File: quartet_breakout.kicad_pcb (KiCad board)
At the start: 2 copper layers, 25.4 x 53.3 mm, 3 parts, among them J1 QUARTET_RECV, J2 QUARTET_RECV, J5 Conn_01x18

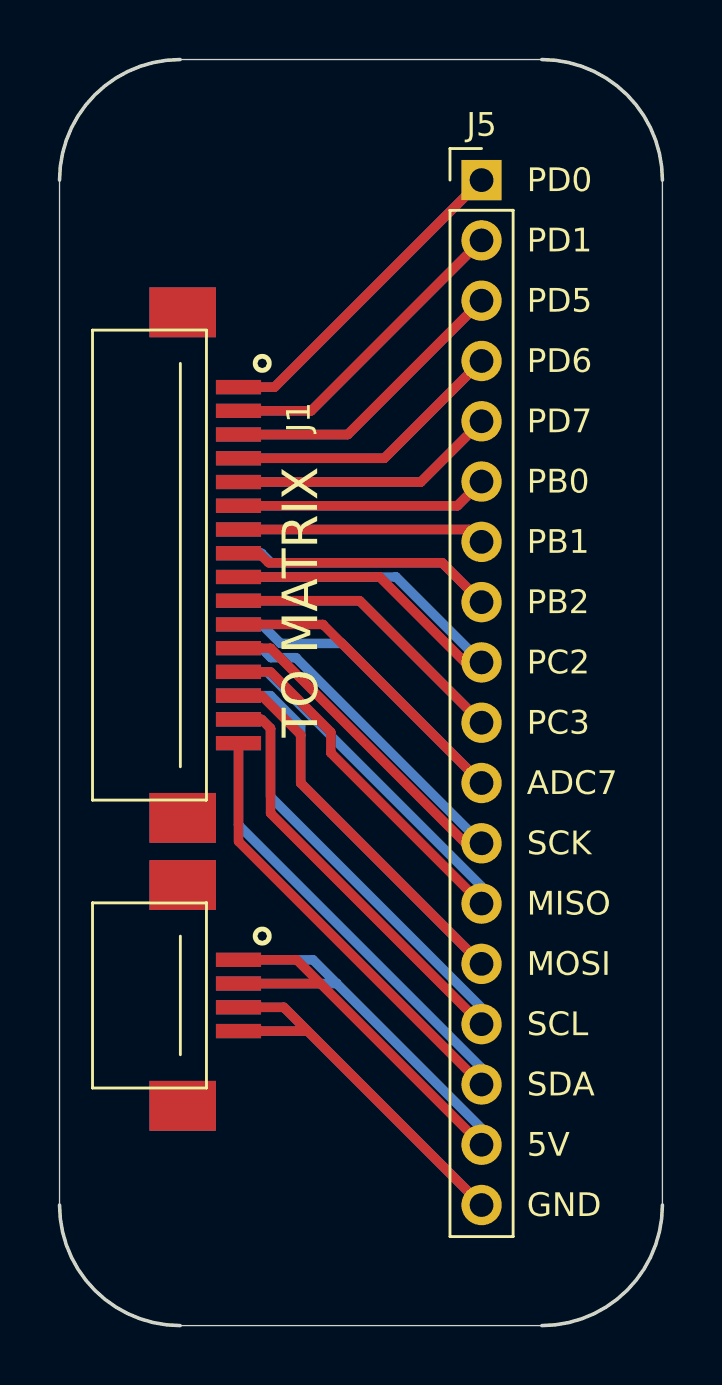
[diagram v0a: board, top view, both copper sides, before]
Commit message: Reroute matrix, redo schematics for feather compat
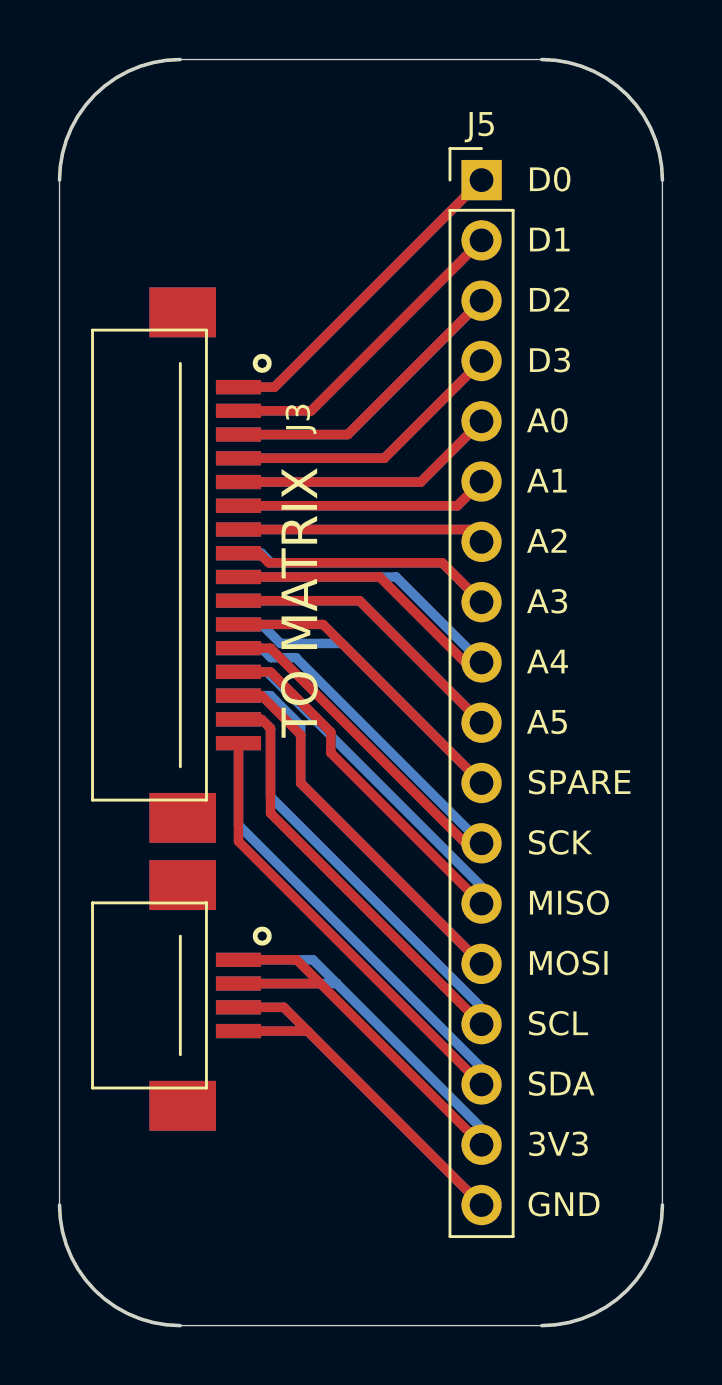
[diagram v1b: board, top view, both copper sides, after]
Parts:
- renumbered J1 to J3
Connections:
- net +5V renamed +3V3
- net ADC7 renamed SPARE
- net PB0 renamed A1
- net PB1 renamed A2
- net PB2 renamed A3
- net PC2 renamed A4
- net PC3 renamed A5
- net PD0 renamed D0
- net PD1 renamed D1
- net PD5 renamed D2
- net PD6 renamed D3
- net PD7 renamed A0
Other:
- board text added: "3V3"
- board text added: "A0"
- board text added: "A1"
- board text added: "A2"
- board text added: "A3"
- board text added: "A4"
- board text added: "A5"
- board text added: "D0"
- board text added: "D1"
- board text added: "D2"
- board text added: "D3"
- board text added: "SPARE"
- board text removed: "5V"
- board text removed: "ADC7"
- board text removed: "PB0"
- board text removed: "PB1"
- board text removed: "PB2"
- board text removed: "PC2"
- board text removed: "PC3"
- board text removed: "PD0"
- board text removed: "PD1"
- board text removed: "PD5"
- board text removed: "PD6"
- board text removed: "PD7"

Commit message: Finish and route quartet mainboard
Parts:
- moved J3 27.3 mm to (68.6, 117.3)
- moved J2 0.23 mm to (68.6, 117.3)
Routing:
- net +3V3: track 34.9 -> 26.8 mm
- net GND: track 33.2 -> 28.2 mm
- net MOSI: track 32.4 -> 31.9 mm
- net SDA: track 37.2 -> 36.7 mm
- added copper zone on F.Cu, net +3V3
- added copper zone on B.Cu, net GND

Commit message: Get ready for JLCPCB
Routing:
- net +3V3: track 26.8 -> 30.7 mm
- net GND: track 28.2 -> 31.7 mm
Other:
- board text added: "JLCJLCJLCJLC"
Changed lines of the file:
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@@
   (general
     (thickness 1.6)
-    (drawings 28)
-    (tracks 88)
+    (drawings 29)
+    (tracks 92)
     (zones 0)
     (modules 3)
@@
       (outputformat 1)
       (mirror false)
-      (drillshape 1)
+      (drillshape 0)
       (scaleselection 1)
-      (outputdirectory ""))
+      (outputdirectory "export_breakout/"))
   )
   (net 0 "")
@@
       (effects (font (size 1 1) (thickness 0.15)) (justify mirror))
     )
+    (fp_line (start -2.4 -6.15) (end -2.4 -1.35) (layer B.SilkS) (width 0.12))
+    (fp_line (start 5.4 -1.35) (end 5.4 -6.15) (layer B.SilkS) (width 0.12))
+    (fp_line (start 5.4 -6.15) (end -2.4 -6.15) (layer B.SilkS) (width 0.12))
+    (fp_line (start 4 -2.45) (end -1 -2.45) (layer B.SilkS) (width 0.12))
+    (fp_line (start 5.4 -1.35) (end -2.4 -1.35) (layer B.SilkS) (width 0.12))
+    (fp_circle (center -1.318 1.048) (end -1.418 1.048) (layer B.SilkS) (width 0.6))
+    (fp_line (start 9.73 -6.15) (end 9.73 -1.35) (layer B.SilkS) (width 0.12))
+    (fp_line (start 28.13 -2.45) (end 11.13 -2.45) (layer B.SilkS) (width 0.12))
+    (fp_line (start 29.53 -1.35) (end 9.73 -1.35) (layer B.SilkS) (width 0.12))
+    (fp_line (start 29.53 -6.15) (end 9.73 -6.15) (layer B.SilkS) (width 0.12))
+    (fp_circle (center 10.874 1.048) (end 10.774 1.048) (layer B.SilkS) (width 0.6))
     (fp_line (start 29.53 -1.35) (end 29.53 -6.15) (layer B.SilkS) (width 0.12))
-    (fp_circle (center 10.874 1.048) (end 10.774 1.048) (layer B.SilkS) (width 0.6))
-    (fp_line (start 29.53 -6.15) (end 9.73 -6.15) (layer B.SilkS) (width 0.12))
-    (fp_line (start 29.53 -1.35) (end 9.73 -1.35) (layer B.SilkS) (width 0.12))
-    (fp_line (start 28.13 -2.45) (end 11.13 -2.45) (layer B.SilkS) (width 0.12))
-    (fp_line (start 9.73 -6.15) (end 9.73 -1.35) (layer B.SilkS) (width 0.12))
-    (fp_circle (center -1.318 1.048) (end -1.418 1.048) (layer B.SilkS) (width 0.6))
-    (fp_line (start 5.4 -1.35) (end -2.4 -1.35) (layer B.SilkS) (width 0.12))
-    (fp_line (start 4 -2.45) (end -1 -2.45) (layer B.SilkS) (width 0.12))
-    (fp_line (start 5.4 -6.15) (end -2.4 -6.15) (layer B.SilkS) (width 0.12))
-    (fp_line (start 5.4 -1.35) (end 5.4 -6.15) (layer B.SilkS) (width 0.12))
-    (fp_line (start -2.4 -6.15) (end -2.4 -1.35) (layer B.SilkS) (width 0.12))
     (pad 15 smd rect (at 13.13 0 270) (size 0.6 1.9) (layers B.Cu B.Paste B.Mask)
       (net 5 SCL))
@@
       (effects (font (size 1 1) (thickness 0.15)))
     )
+    (fp_line (start -29.53 1.35) (end -29.53 6.15) (layer F.SilkS) (width 0.12))
+    (fp_circle (center -28.13 -1) (end -28.03 -1) (layer F.SilkS) (width 0.6))
+    (fp_line (start -29.53 6.15) (end -9.73 6.15) (layer F.SilkS) (width 0.12))
+    (fp_line (start -29.53 1.35) (end -9.73 1.35) (layer F.SilkS) (width 0.12))
+    (fp_line (start -28.13 2.45) (end -11.13 2.45) (layer F.SilkS) (width 0.12))
+    (fp_line (start -9.73 6.15) (end -9.73 1.35) (layer F.SilkS) (width 0.12))
+    (fp_circle (center -4 -1) (end -3.9 -1) (layer F.SilkS) (width 0.6))
+    (fp_line (start -5.4 1.35) (end 2.4 1.35) (layer F.SilkS) (width 0.12))
+    (fp_line (start -4 2.45) (end 1 2.45) (layer F.SilkS) (width 0.12))
+    (fp_line (start -5.4 6.15) (end 2.4 6.15) (layer F.SilkS) (width 0.12))
+    (fp_line (start -5.4 1.35) (end -5.4 6.15) (layer F.SilkS) (width 0.12))
     (fp_line (start 2.4 6.15) (end 2.4 1.35) (layer F.SilkS) (width 0.12))
-    (fp_line (start -5.4 1.35) (end -5.4 6.15) (layer F.SilkS) (width 0.12))
-    (fp_line (start -5.4 6.15) (end 2.4 6.15) (layer F.SilkS) (width 0.12))
-    (fp_line (start -4 2.45) (end 1 2.45) (layer F.SilkS) (width 0.12))
-    (fp_line (start -5.4 1.35) (end 2.4 1.35) (layer F.SilkS) (width 0.12))
-    (fp_circle (center -4 -1) (end -3.9 -1) (layer F.SilkS) (width 0.6))
-    (fp_line (start -9.73 6.15) (end -9.73 1.35) (layer F.SilkS) (width 0.12))
-    (fp_line (start -28.13 2.45) (end -11.13 2.45) (layer F.SilkS) (width 0.12))
-    (fp_line (start -29.53 1.35) (end -9.73 1.35) (layer F.SilkS) (width 0.12))
-    (fp_line (start -29.53 6.15) (end -9.73 6.15) (layer F.SilkS) (width 0.12))
-    (fp_circle (center -28.13 -1) (end -28.03 -1) (layer F.SilkS) (width 0.6))
-    (fp_line (start -29.53 1.35) (end -29.53 6.15) (layer F.SilkS) (width 0.12))
     (pad 17 smd rect (at -3 0 270) (size 0.6 1.9) (layers F.Cu F.Paste F.Mask)
       (net 18 +3V3))
@@
       (effects (font (size 1 1) (thickness 0.15)))
     )
+    (fp_line (start 1.8 -1.8) (end -1.8 -1.8) (layer F.CrtYd) (width 0.05))
+    (fp_line (start 1.8 44.95) (end 1.8 -1.8) (layer F.CrtYd) (width 0.05))
+    (fp_line (start -1.8 44.95) (end 1.8 44.95) (layer F.CrtYd) (width 0.05))
+    (fp_line (start -1.8 -1.8) (end -1.8 44.95) (layer F.CrtYd) (width 0.05))
+    (fp_line (start -1.33 -1.33) (end 0 -1.33) (layer F.SilkS) (width 0.12))
+    (fp_line (start -1.33 0) (end -1.33 -1.33) (layer F.SilkS) (width 0.12))
+    (fp_line (start -1.33 1.27) (end 1.33 1.27) (layer F.SilkS) (width 0.12))
+    (fp_line (start 1.33 1.27) (end 1.33 44.51) (layer F.SilkS) (width 0.12))
+    (fp_line (start -1.33 1.27) (end -1.33 44.51) (layer F.SilkS) (width 0.12))
+    (fp_line (start -1.33 44.51) (end 1.33 44.51) (layer F.SilkS) (width 0.12))
+    (fp_line (start -1.27 -0.635) (end -0.635 -1.27) (layer F.Fab) (width 0.1))
+    (fp_line (start -1.27 44.45) (end -1.27 -0.635) (layer F.Fab) (width 0.1))
+    (fp_line (start 1.27 44.45) (end -1.27 44.45) (layer F.Fab) (width 0.1))
+    (fp_line (start 1.27 -1.27) (end 1.27 44.45) (layer F.Fab) (width 0.1))
+    (fp_line (start -0.635 -1.27) (end 1.27 -1.27) (layer F.Fab) (width 0.1))
     (fp_text user %R (at 0 21.59 90) (layer F.Fab)
       (effects (font (size 1 1) (thickness 0.15)))
     )
-    (fp_line (start -0.635 -1.27) (end 1.27 -1.27) (layer F.Fab) (width 0.1))
-    (fp_line (start 1.27 -1.27) (end 1.27 44.45) (layer F.Fab) (width 0.1))
-    (fp_line (start 1.27 44.45) (end -1.27 44.45) (layer F.Fab) (width 0.1))
-    (fp_line (start -1.27 44.45) (end -1.27 -0.635) (layer F.Fab) (width 0.1))
-    (fp_line (start -1.27 -0.635) (end -0.635 -1.27) (layer F.Fab) (width 0.1))
-    (fp_line (start -1.33 44.51) (end 1.33 44.51) (layer F.SilkS) (width 0.12))
-    (fp_line (start -1.33 1.27) (end -1.33 44.51) (layer F.SilkS) (width 0.12))
-    (fp_line (start 1.33 1.27) (end 1.33 44.51) (layer F.SilkS) (width 0.12))
-    (fp_line (start -1.33 1.27) (end 1.33 1.27) (layer F.SilkS) (width 0.12))
-    (fp_line (start -1.33 0) (end -1.33 -1.33) (layer F.SilkS) (width 0.12))
-    (fp_line (start -1.33 -1.33) (end 0 -1.33) (layer F.SilkS) (width 0.12))
-    (fp_line (start -1.8 -1.8) (end -1.8 44.95) (layer F.CrtYd) (width 0.05))
-    (fp_line (start -1.8 44.95) (end 1.8 44.95) (layer F.CrtYd) (width 0.05))
-    (fp_line (start 1.8 44.95) (end 1.8 -1.8) (layer F.CrtYd) (width 0.05))
-    (fp_line (start 1.8 -1.8) (end -1.8 -1.8) (layer F.CrtYd) (width 0.05))
     (pad 18 thru_hole oval (at 0 43.18) (size 1.7 1.7) (drill 1) (layers *.Cu *.Mask)
       (net 1 GND))
@@
     )
   )
+  (gr_text JLCJLCJLCJLC (at 64.008 97.028 90) (layer F.SilkS)
+    (effects (font (size 0.8 0.8) (thickness 0.15)))
+  )
   (gr_line (start 60.96 81.28) (end 60.96 124.46) (layer Edge.Cuts) (width 0.05))
   (gr_line (start 81.28 76.2) (end 66.04 76.2) (layer Edge.Cuts) (width 0.05))
@@
   (segment (start 71.628 117.348) (end 68.58 117.348) (width 0.4) (layer B.Cu) (net 1))
   (segment (start 68.58 117.348) (end 68.58 116.348) (width 0.4) (layer B.Cu) (net 1))
+  (segment (start 70.628 116.348) (end 71.628 117.348) (width 0.4) (layer F.Cu) (net 1))
+  (segment (start 68.58 116.348) (end 70.628 116.348) (width 0.4) (layer F.Cu) (net 1))
   (segment (start 70.738 101.218) (end 78.74 109.22) (width 0.4) (layer F.Cu) (net 2))
   (segment (start 68.58 101.218) (end 70.738 101.218) (width 0.4) (layer F.Cu) (net 2))
@@
   (segment (start 72.136 115.316) (end 72.104 115.348) (width 0.4) (layer B.Cu) (net 18))
   (segment (start 68.58 114.348) (end 68.58 115.348) (width 0.4) (layer B.Cu) (net 18))
+  (segment (start 71.168 114.348) (end 72.136 115.316) (width 0.4) (layer B.Cu) (net 18))
+  (segment (start 68.58 114.348) (end 71.168 114.348) (width 0.4) (layer B.Cu) (net 18))
   (zone (net 18) (net_name +3V3) (layer F.Cu) (hatch edge 0.508)
     (connect_pads (clearance 0.508))
